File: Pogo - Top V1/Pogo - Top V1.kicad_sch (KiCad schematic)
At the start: 1 part, among them J1 Conn_01x02_Socket

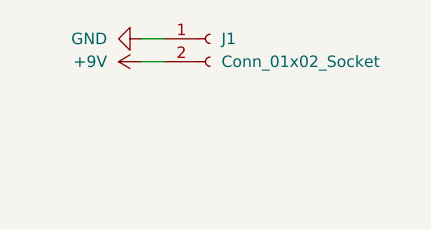
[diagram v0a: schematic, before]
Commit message: Finally fixed the issues with folder and file naming.
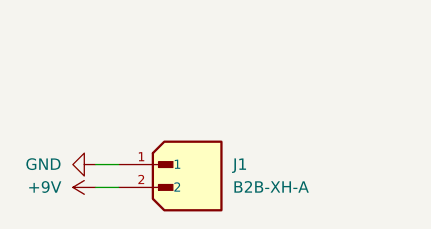
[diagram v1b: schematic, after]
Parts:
- removed J1: Conn_01x02_Socket, Connector_AMASS:AMASS_XT30U-M_1x02_P5.0mm_Vertical, symbol Connector:Conn_01x02_Socket
- added J1: B2B-XH-A, B2B-XH-A:B2B-XH-A, symbol B2B-XH-A:B2B-XH-A
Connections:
- net +9V: now also J1.2
- net GND: now also J1.1
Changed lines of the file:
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@@
 	(wire
 		(pts
-			(xy 151.13 86.36) (xy 153.67 86.36)
+			(xy 146.05 100.33) (xy 148.59 100.33)
 		)
 		(stroke
@@
 	(wire
 		(pts
-			(xy 151.13 88.9) (xy 153.67 88.9)
+			(xy 146.05 102.87) (xy 148.59 102.87)
 		)
 		(stroke
@@
 	)
 	(symbol
-		(lib_id "Connector:Conn_01x02_Socket")
-		(at 158.75 86.36 0)
+		(lib_id "power:GND")
+		(at 146.05 100.33 270)
+		(unit 1)
+		(exclude_from_sim no)
+		(in_bom yes)
+		(on_board yes)
+		(dnp no)
+		(fields_autoplaced yes)
+		(property "Reference" "#PWR01"
+			(at 139.7 100.33 0)
+			(effects
+				(font
+					(size 1.27 1.27)
+				)
+				(hide yes)
+			)
+		)
+		(property "Value" "GND"
+			(at 142.24 100.3299 90)
+			(effects
+				(font
+					(size 1.27 1.27)
+				)
+				(justify right)
+			)
+		)
+		(property "Footprint" ""
+			(at 146.05 100.33 0)
+			(effects
+				(font
+					(size 1.27 1.27)
+				)
+				(hide yes)
+			)
+		)
+		(property "Datasheet" ""
+			(at 146.05 100.33 0)
+			(effects
+				(font
+					(size 1.27 1.27)
+				)
+				(hide yes)
+			)
+		)
+		(property "Description" "Power symbol creates a global label with name \"GND\" , ground"
+			(at 146.05 100.33 0)
+			(effects
+				(font
+					(size 1.27 1.27)
+				)
+				(hide yes)
+			)
+		)
+		(pin "1"
+		)
+		(instances
+			(project ""
+				(path "/f2fb824b-0c7c-4faa-907c-a8c85c24ff79"
+					(reference "#PWR01")
+					(unit 1)
+				)
+			)
+		)
+	)
+	(symbol
+		(lib_id "power:+9V")
+		(at 146.05 102.87 90)
+		(unit 1)
+		(exclude_from_sim no)
+		(in_bom yes)
+		(on_board yes)
+		(dnp no)
+		(fields_autoplaced yes)
+		(property "Reference" "#PWR02"
+			(at 149.86 102.87 0)
+			(effects
+				(font
+					(size 1.27 1.27)
+				)
+				(hide yes)
+			)
+		)
+		(property "Value" "+9V"
+			(at 142.24 102.8699 90)
+			(effects
+				(font
+					(size 1.27 1.27)
+				)
+				(justify left)
+			)
+		)
+		(property "Footprint" ""
+			(at 146.05 102.87 0)
+			(effects
+				(font
+					(size 1.27 1.27)
+				)
+				(hide yes)
+			)
+		)
+		(property "Datasheet" ""
+			(at 146.05 102.87 0)
+			(effects
+				(font
+					(size 1.27 1.27)
+				)
+				(hide yes)
+			)
+		)
+		(property "Description" "Power symbol creates a global label with name \"+9V\""
+			(at 146.05 102.87 0)
+			(effects
+				(font
+					(size 1.27 1.27)
+				)
+				(hide yes)
+			)
+		)
+		(pin "1"
+		)
+		(instances
+			(project ""
+				(path "/f2fb824b-0c7c-4faa-907c-a8c85c24ff79"
+					(reference "#PWR02")
+					(unit 1)
+				)
+			)
+		)
+	)
+	(symbol
+		(lib_id "B2B-XH-A:B2B-XH-A")
+		(at 156.21 102.87 0)
 		(unit 1)
 		(exclude_from_sim no)
@@
 		(fields_autoplaced yes)
 		(property "Reference" "J1"
-			(at 160.02 86.3599 0)
+			(at 161.29 100.3299 0)
 			(effects
 				(font
@@
 			)
 		)
-		(property "Value" "Conn_01x02_Socket"
-			(at 160.02 88.8999 0)
+		(property "Value" "B2B-XH-A"
+			(at 161.29 102.8699 0)
 			(effects
 				(font
@@
 			)
 		)
-		(property "Footprint" "Connector_AMASS:AMASS_XT30U-M_1x02_P5.0mm_Vertical"
-			(at 158.75 86.36 0)
-			(effects
-				(font
-					(size 1.27 1.27)
-				)
-				(hide yes)
-			)
-		)
-		(property "Datasheet" "https://www.tme.com/Document/7d9d972ae3468777f69ec2ee99897652/XT30U-M.pdf"
-			(at 158.75 86.36 0)
-			(effects
-				(font
-					(size 1.27 1.27)
-				)
-				(hide yes)
-			)
-		)
-		(property "Description" "2 PIN XT30 Male"
-			(at 158.75 86.36 0)
-			(effects
-				(font
-					(size 1.27 1.27)
-				)
-				(hide yes)
-			)
-		)
-		(property "Mfr." "TME"
-			(at 158.75 86.36 0)
-			(effects
-				(font
-					(size 1.27 1.27)
-				)
-				(hide yes)
-			)
-		)
-		(property "Part #" "XT30U-M"
-			(at 158.75 86.36 0)
-			(effects
-				(font
-					(size 1.27 1.27)
-				)
-				(hide yes)
-			)
-		)
-		(property "Order Link" "https://www.tme.com/us/en-us/details/xt30u-m/dc-power-connectors/amass/"
-			(at 158.75 86.36 0)
-			(effects
-				(font
-					(size 1.27 1.27)
-				)
-				(hide yes)
-			)
-		)
-		(property "Price" "$0.626"
-			(at 158.75 86.36 0)
-			(effects
-				(font
-					(size 1.27 1.27)
-				)
+		(property "Footprint" "B2B-XH-A:B2B-XH-A"
+			(at 156.21 102.87 0)
+			(effects
+				(font
+					(size 1.27 1.27)
+				)
+				(justify bottom)
+				(hide yes)
+			)
+		)
+		(property "Datasheet" ""
+			(at 156.21 102.87 0)
+			(effects
+				(font
+					(size 1.27 1.27)
+				)
+				(hide yes)
+			)
+		)
+		(property "Description" ""
+			(at 156.21 102.87 0)
+			(effects
+				(font
+					(size 1.27 1.27)
+				)
+				(hide yes)
+			)
+		)
+		(property "PARTREV" "N/A"
+			(at 156.21 102.87 0)
+			(effects
+				(font
+					(size 1.27 1.27)
+				)
+				(justify bottom)
+				(hide yes)
+			)
+		)
+		(property "STANDARD" "Manufacturer Recommendations"
+			(at 156.21 102.87 0)
+			(effects
+				(font
+					(size 1.27 1.27)
+				)
+				(justify bottom)
+				(hide yes)
+			)
+		)
+		(property "MAXIMUM_PACKAGE_HEIGHT" "7 mm"
+			(at 156.21 102.87 0)
+			(effects
+				(font
+					(size 1.27 1.27)
+				)
+				(justify bottom)
+				(hide yes)
+			)
+		)
+		(property "MANUFACTURER" "JST Sales America Inc."
+			(at 156.21 102.87 0)
+			(effects
+				(font
+					(size 1.27 1.27)
+				)
+				(justify bottom)
 				(hide yes)
 			)
@@
 		(instances
 			(project ""
-				(path "/3290a135-58b8-4768-b0c2-c03f3bc7cf69"
+				(path "/f2fb824b-0c7c-4faa-907c-a8c85c24ff79"
 					(reference "J1")
 					(unit 1)
 				)
-			)
-		)
-	)
-	(symbol
-		(lib_id "power:+9V")
-		(at 151.13 88.9 90)
-		(unit 1)
-		(exclude_from_sim no)
-		(in_bom yes)
-		(on_board yes)
-		(dnp no)
-		(fields_autoplaced yes)
-		(property "Reference" "#PWR02"
-			(at 154.94 88.9 0)
-			(effects
-				(font
-					(size 1.27 1.27)
-				)
-				(hide yes)
-			)
-		)
-		(property "Value" "+9V"
-			(at 147.32 88.8999 90)
-			(effects
-				(font
-					(size 1.27 1.27)
-				)
-				(justify left)
-			)
-		)
-		(property "Footprint" ""
-			(at 151.13 88.9 0)
-			(effects
-				(font
-					(size 1.27 1.27)
-				)
-				(hide yes)
-			)
-		)
-		(property "Datasheet" ""
-			(at 151.13 88.9 0)
-			(effects
-				(font
-					(size 1.27 1.27)
-				)
-				(hide yes)
-			)
-		)
-		(property "Description" "Power symbol creates a global label with name \"+9V\""
-			(at 151.13 88.9 0)
-			(effects
-				(font
-					(size 1.27 1.27)
-				)
-				(hide yes)
-			)
-		)
-		(pin "1"
-		)
-		(instances
-			(project ""
-				(path "/3290a135-58b8-4768-b0c2-c03f3bc7cf69"
-					(reference "#PWR02")
-					(unit 1)
-				)
-			)
-		)
-	)
-	(symbol
-		(lib_id "power:GND")
-		(at 151.13 86.36 270)
-		(unit 1)
-		(exclude_from_sim no)
-		(in_bom yes)
-		(on_board yes)
-		(dnp no)
-		(fields_autoplaced yes)
-		(property "Reference" "#PWR01"
-			(at 144.78 86.36 0)
-			(effects
-				(font
-					(size 1.27 1.27)
-				)
-				(hide yes)
-			)
-		)
-		(property "Value" "GND"
-			(at 147.32 86.3599 90)
-			(effects
-				(font
-					(size 1.27 1.27)
-				)
-				(justify right)
-			)
-		)
-		(property "Footprint" ""
-			(at 151.13 86.36 0)
-			(effects
-				(font
-					(size 1.27 1.27)
-				)
-				(hide yes)
-			)
-		)
-		(property "Datasheet" ""
-			(at 151.13 86.36 0)
-			(effects
-				(font
-					(size 1.27 1.27)
-				)
-				(hide yes)
-			)
-		)
-		(property "Description" "Power symbol creates a global label with name \"GND\" , ground"
-			(at 151.13 86.36 0)
-			(effects
-				(font
-					(size 1.27 1.27)
-				)
-				(hide yes)
-			)
-		)
-		(pin "1"
-		)
-		(instances
-			(project ""
-				(path "/3290a135-58b8-4768-b0c2-c03f3bc7cf69"
-					(reference "#PWR01")
-					(unit 1)
-				)

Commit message: Created interactive BOMs for Pogo and pad boards.
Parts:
- J1: MANUFACTURER JST Sales America Inc. -> (none); MAXIMUM_PACKAGE_HEIGHT 7 mm -> (none); Mfr. (none) -> JST Sales America Inc.; Order Link (none) -> https://www.digikey.com/en/products/detail/jst-sales-americ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; PARTREV N/A -> (none); Part # (none) -> B2B-XH-A-GU; Price (none) -> $0.24; STANDARD Manufacturer Recommendations -> (none)
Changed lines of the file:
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@@
 			)
 		)
-		(property "Datasheet" ""
+		(property "Datasheet" "https://www.jst-mfg.com/product/pdf/eng/eXH.pdf"
 			(at 156.21 102.87 0)
 			(effects
@@
 			)
 		)
-		(property "Description" ""
+		(property "Description" "CONN HEADER VERT 2POS 2.5MM"
 			(at 156.21 102.87 0)
 			(effects
@@
 			)
 		)
-		(property "PARTREV" "N/A"
+		(property "Mfr." "JST Sales America Inc."
 			(at 156.21 102.87 0)
 			(effects
@@
 			)
 		)
-		(property "STANDARD" "Manufacturer Recommendations"
+		(property "Part #" "B2B-XH-A-GU"
 			(at 156.21 102.87 0)
 			(effects
@@
 					(size 1.27 1.27)
 				)
-				(justify bottom)
 				(hide yes)
 			)
 		)
-		(property "MAXIMUM_PACKAGE_HEIGHT" "7 mm"
+		(property "Order Link" "https://www.digikey.com/en/products/detail/jst-sales-america-inc/B2B-XH-A-GU/2043065"
 			(at 156.21 102.87 0)
 			(effects
@@
 					(size 1.27 1.27)
 				)
-				(justify bottom)
 				(hide yes)
 			)
 		)
-		(property "MANUFACTURER" "JST Sales America Inc."
+		(property "Price" "$0.24"
 			(at 156.21 102.87 0)
 			(effects
@@
 					(size 1.27 1.27)
 				)
-				(justify bottom)
 				(hide yes)
 			)
